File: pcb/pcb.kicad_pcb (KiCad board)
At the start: 2 copper layers, 109 x 54 mm, 63 parts, among them J1 MALE, J10 TC2030_NL, J101 MALE, J102 FEMALE, J103 MALE, J104 FEMALE, J105 MALE, J106 FEMALE, J107 MALE, J108 FEMALE, J11 STANDOFF, J111 STANDOFF, J112 STANDOFF, J113 STANDOFF, J114 STANDOFF, J12 STANDOFF, J13 STANDOFF, J14 STANDOFF, J2 FEMALE, J3 MALE, J4 FEMALE, J5 MALE, J6 FEMALE, J7 MALE, J8 FEMALE, J9 DTR, Q1 2N3904, SW1 ACTION, SW2 ACTION, SW3 ACTION, SW4 ACTION, U3 ATmega328P-MU, Y1 YSX321SL

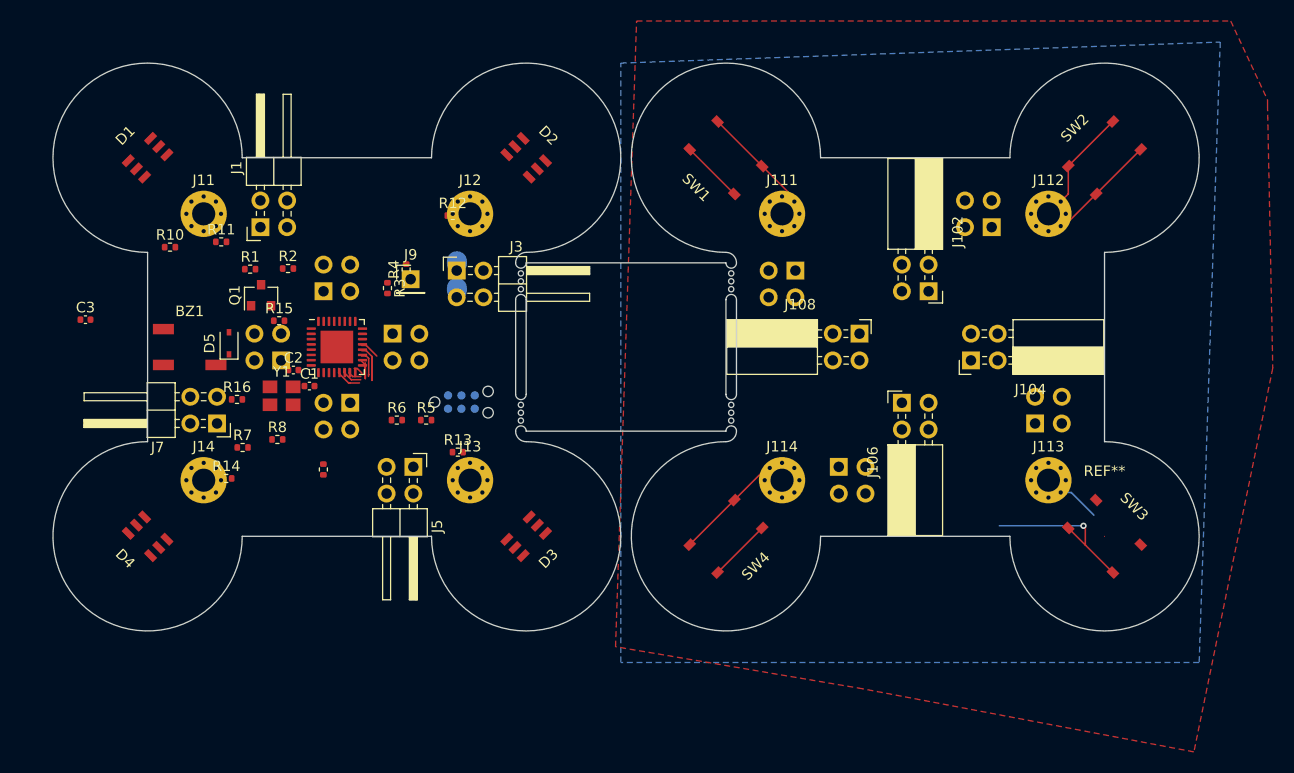
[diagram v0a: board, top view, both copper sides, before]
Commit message: Update solder mask keep out
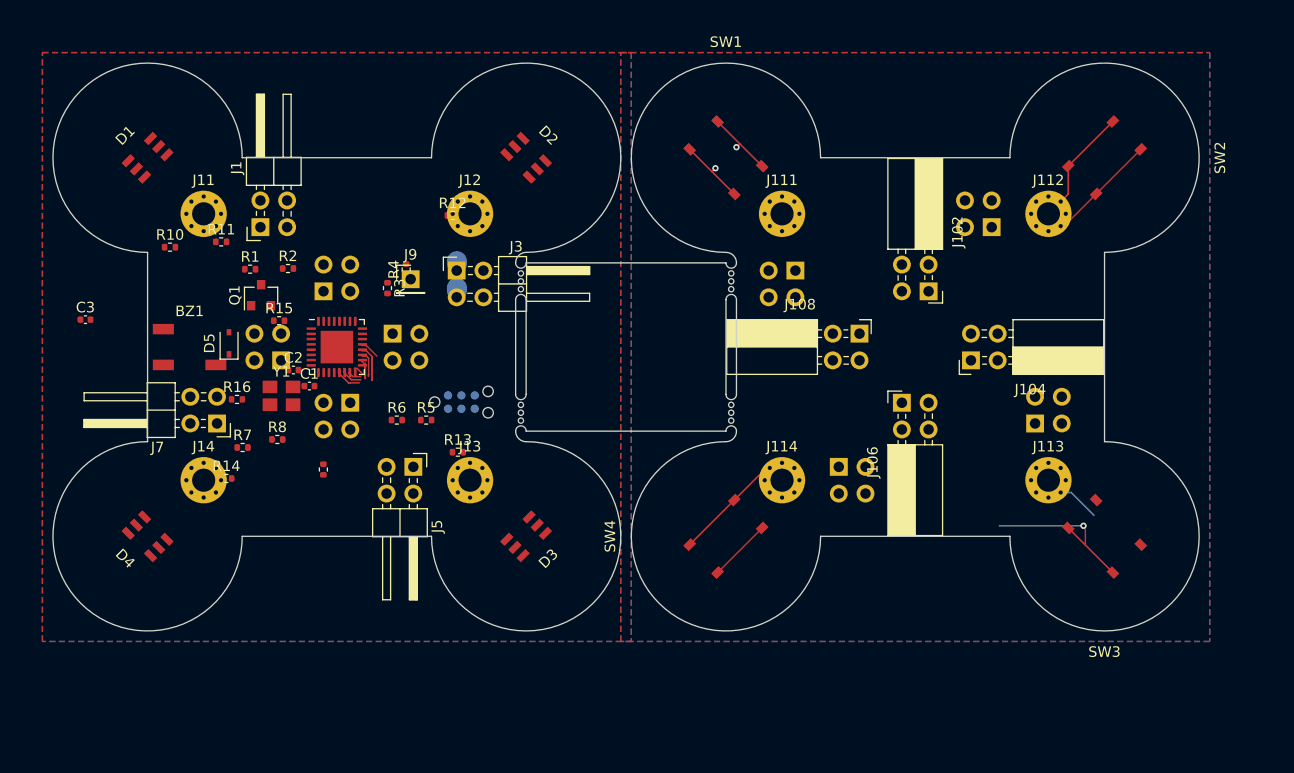
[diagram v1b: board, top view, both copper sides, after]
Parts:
- removed REF**: Leaf, node:Leaf
- SW1, SW2, SW3, SW4: footprint node:TS-1187A-B-A-B -> node:top-leaf
- turned SW1 to 0 degrees
- turned SW2 to 270 degrees
- turned SW3 to 180 degrees
- turned SW4 to 90 degrees
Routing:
- net Net-(J111-Pad1): track 16.6 -> 6.78 mm, vias 0 -> 1
- net GND: track 15.9 -> 22.4 mm, vias 1 -> 2
- added copper zone on B.Cu, net GNDB
- added copper zone on F.Cu, net GNDB
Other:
- rule pad_to_mask_clearance: 0.051 -> 0

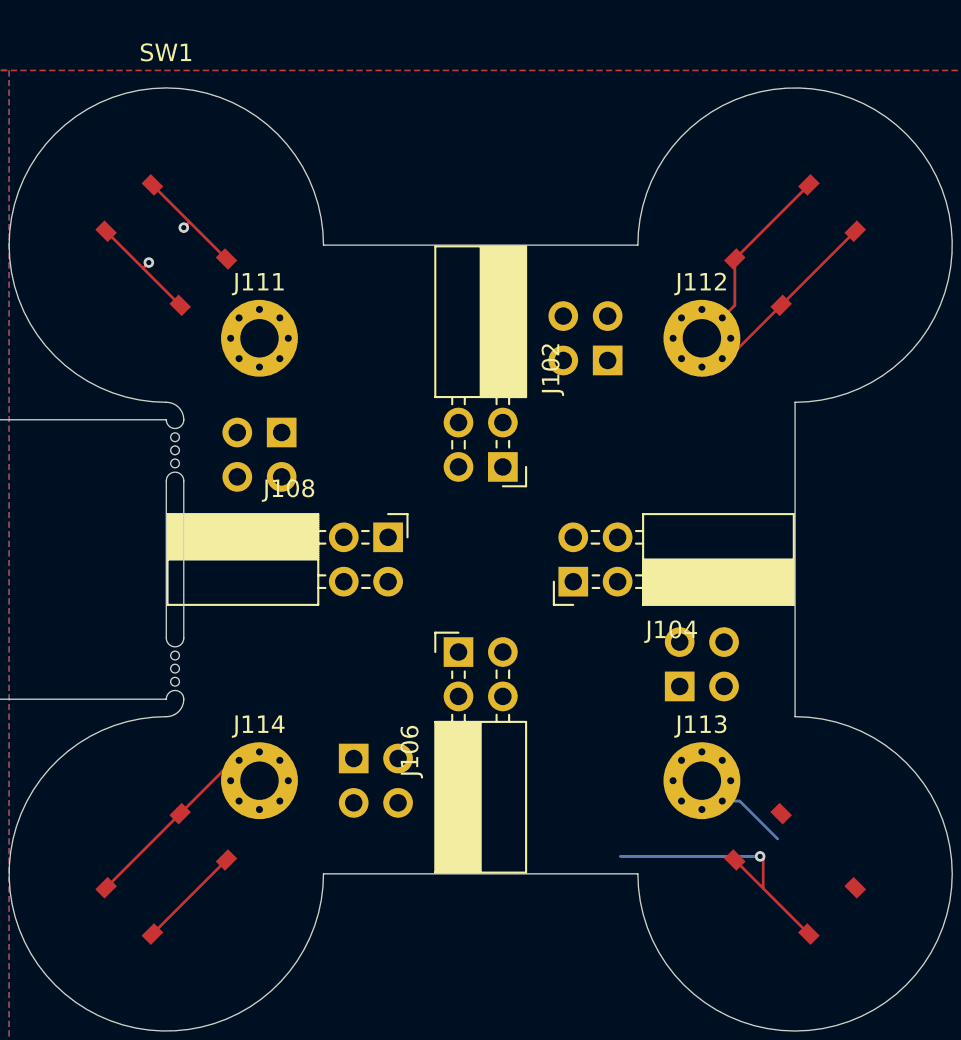
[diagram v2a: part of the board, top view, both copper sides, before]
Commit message: Route top board
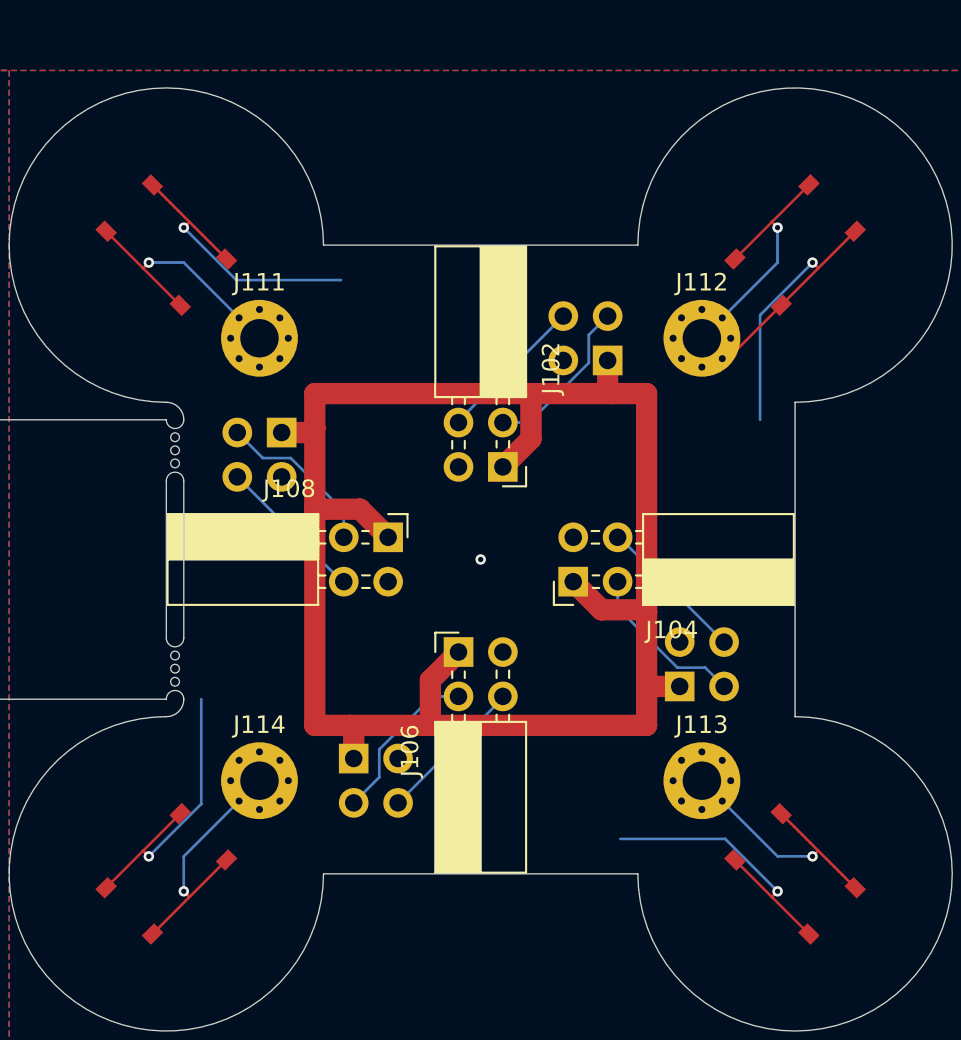
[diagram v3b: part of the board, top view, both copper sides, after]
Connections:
- J101 pad 1: Net-(J101-Pad1) -> +5V
- J102 pad 1: Net-(J101-Pad1) -> +5V
- J103 pad 1: Net-(J103-Pad1) -> +5V
- J104 pad 1: Net-(J103-Pad1) -> +5V
- J105 pad 1: Net-(J105-Pad1) -> +5V
- J106 pad 1: Net-(J105-Pad1) -> +5V
- J107 pad 1: Net-(J107-Pad1) -> +5V
- J108 pad 1: Net-(J107-Pad1) -> +5V
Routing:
- net +5V: track 0.00 -> 103.8 mm
- net GND: track 22.4 -> 50.1 mm, vias 2 -> 4
- net Net-(J112-Pad1): track 22.0 -> 35.9 mm, vias 0 -> 2
- net Net-(J113-Pad1): track 4.38 -> 14.9 mm, vias 0 -> 1
- net Net-(J107-Pad2): track 0.00 -> 9.46 mm
- net Net-(J105-Pad2): track 0.00 -> 9.46 mm
- net Net-(J103-Pad2): track 0.00 -> 9.46 mm
- net Net-(J101-Pad2): track 0.00 -> 9.46 mm
- net Net-(J107-Pad4): track 0.00 -> 8.58 mm
- net Net-(J105-Pad4): track 0.00 -> 8.58 mm
- net Net-(J103-Pad4): track 0.00 -> 8.58 mm
- net Net-(J101-Pad4): track 0.00 -> 8.58 mm
- net Net-(J111-Pad1): track 6.78 -> 13.3 mm
- net Net-(J114-Pad1): track 16.6 -> 14.9 mm, vias 0 -> 1

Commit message: Reduce footprint of tab
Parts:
- removed the mouse-bite at (138.5, 98.8)
- removed the mouse-bite at (158.5, 98.8)
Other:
- outline, holes or cut-outs redrawn
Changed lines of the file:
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@@
   (general
     (thickness 1)
-    (drawings 104)
+    (drawings 112)
     (tracks 141)
     (zones 0)
-    (modules 62)
+    (modules 60)
     (nets 70)
   )
@@
   (layers
     (0 F.Cu signal)
-    (31 B.Cu signal)
+    (31 B.Cu signal hide)
     (32 B.Adhes user hide)
     (33 F.Adhes user hide)
@@
     (38 B.Mask user hide)
     (39 F.Mask user hide)
-    (40 Dwgs.User user)
+    (40 Dwgs.User user hide)
     (41 Cmts.User user hide)
     (42 Eco1.User user hide)
@@
   )
   (module node:mouse-bite (layer F.Cu)
-    (at 138.5 98.75 90)
-    (fp_text reference mouse-bite (at 0 1.524 90) (layer F.SilkS) hide
-      (effects (font (size 1 1) (thickness 0.2)))
-    )
-    (fp_text value VAL** (at 0 -1.524 90) (layer F.SilkS) hide
-      (effects (font (size 1 1) (thickness 0.2)))
-    )
-    (fp_arc (start -1.75 0) (end -1.75 0.5) (angle -180) (layer Eco1.User) (width 0.1016))
-    (fp_arc (start 1.75 0) (end 1.75 -0.5) (angle -180) (layer Eco1.User) (width 0.1016))
-    (pad "" np_thru_hole circle (at 0 0 90) (size 0.5 0.5) (drill 0.5) (layers *.Cu *.Mask))
-    (pad "" np_thru_hole circle (at 0.75 0 90) (size 0.5 0.5) (drill 0.5) (layers *.Cu *.Mask))
-    (pad "" np_thru_hole circle (at -0.75 0 90) (size 0.5 0.5) (drill 0.5) (layers *.Cu *.Mask))
-  )
-  (module node:mouse-bite (layer F.Cu)
-    (at 158.5 98.75 90)
-    (fp_text reference mouse-bite (at 0 1.524 90) (layer F.SilkS) hide
-      (effects (font (size 1 1) (thickness 0.2)))
-    )
-    (fp_text value VAL** (at 0 -1.524 90) (layer F.SilkS) hide
-      (effects (font (size 1 1) (thickness 0.2)))
-    )
-    (fp_arc (start -1.75 0) (end -1.75 0.5) (angle -180) (layer Eco1.User) (width 0.1016))
-    (fp_arc (start 1.75 0) (end 1.75 -0.5) (angle -180) (layer Eco1.User) (width 0.1016))
-    (pad "" np_thru_hole circle (at 0 0 90) (size 0.5 0.5) (drill 0.5) (layers *.Cu *.Mask))
-    (pad "" np_thru_hole circle (at 0.75 0 90) (size 0.5 0.5) (drill 0.5) (layers *.Cu *.Mask))
-    (pad "" np_thru_hole circle (at -0.75 0 90) (size 0.5 0.5) (drill 0.5) (layers *.Cu *.Mask))
-  )
-  (module node:mouse-bite (layer F.Cu)
     (at 158.5 111.25 90)
     (fp_text reference mouse-bite (at 0 1.524 90) (layer F.SilkS) hide
@@
       (net 64 "Net-(J114-Pad1)"))
   )
-  (gr_line (start 158 113) (end 139 113) (layer Edge.Cuts) (width 0.05))
-  (gr_line (start 139 97) (end 158 97) (layer Edge.Cuts) (width 0.05))
-  (gr_line (start 138 100.5) (end 138 109.5) (layer Edge.Cuts) (width 0.05))
-  (gr_line (start 139 109.5) (end 139 100.5) (layer Edge.Cuts) (width 0.05))
-  (gr_line (start 159 100.5) (end 159 109.5) (layer Edge.Cuts) (width 0.05))
-  (gr_line (start 158 109.5) (end 158 100.5) (layer Edge.Cuts) (width 0.05))
-  (gr_arc (start 158.5 113) (end 159 113) (angle -180) (layer Edge.Cuts) (width 0.05))
-  (gr_arc (start 158.5 100.5) (end 159 100.5) (angle -180) (layer Edge.Cuts) (width 0.05))
-  (gr_arc (start 138.5 100.5) (end 139 100.5) (angle -180) (layer Edge.Cuts) (width 0.05))
-  (gr_arc (start 138.5 113) (end 139 113) (angle -180) (layer Edge.Cuts) (width 0.05))
-  (gr_line (start 130 123) (end 112 123) (layer Edge.Cuts) (width 0.05))
-  (gr_line (start 103 114) (end 103 96) (layer Edge.Cuts) (width 0.05))
-  (gr_line (start 112 87) (end 130 87) (layer Edge.Cuts) (width 0.05))
-  (gr_arc (start 103 87) (end 112 87) (angle -270) (layer Edge.Cuts) (width 0.05))
-  (gr_line (start 167 87) (end 185 87) (layer Edge.Cuts) (width 0.05))
-  (gr_line (start 194 96) (end 194 114) (layer Edge.Cuts) (width 0.05))
-  (gr_line (start 185 123) (end 167 123) (layer Edge.Cuts) (width 0.05))
-  (gr_arc (start 103 123) (end 102.999999 113.999999) (angle -270) (layer Edge.Cuts) (width 0.05))
-  (gr_arc (start 139 123) (end 130 123) (angle -270) (layer Edge.Cuts) (width 0.05))
-  (gr_arc (start 139 86.999999) (end 139 96) (angle -270) (layer Edge.Cuts) (width 0.05))
-  (gr_arc (start 139 97) (end 139 96) (angle -90) (layer Edge.Cuts) (width 0.05))
-  (gr_arc (start 158 87) (end 167 87) (angle -270) (layer Edge.Cuts) (width 0.05))
-  (gr_arc (start 158 123) (end 157.999999 113.999999) (angle -270) (layer Edge.Cuts) (width 0.05))
-  (gr_arc (start 194 123) (end 185 123) (angle -270) (layer Edge.Cuts) (width 0.05))
-  (gr_arc (start 194 86.999999) (end 194 96) (angle -270) (layer Edge.Cuts) (width 0.05))
-  (gr_arc (start 158 113) (end 158 114) (angle -90) (layer Edge.Cuts) (width 0.05))
-  (gr_arc (start 139 113) (end 138 113) (angle -90) (layer Edge.Cuts) (width 0.05))
-  (gr_arc (start 158 97) (end 159 97) (angle -90) (layer Edge.Cuts) (width 0.05))
-  (gr_arc (start 138.5 97) (end 138 97) (angle -180) (layer Edge.Cuts) (width 0.05))
-  (gr_arc (start 158.5 97) (end 158 97) (angle -180) (layer Edge.Cuts) (width 0.05))
-  (gr_arc (start 158.5 109.5) (end 158 109.5) (angle -180) (layer Edge.Cuts) (width 0.05))
-  (gr_arc (start 138.5 109.5) (end 138 109.5) (angle -180) (layer Edge.Cuts) (width 0.05))
+  (gr_line (start 158.050126 109.5) (end 139.050126 109.5) (layer Edge.Cuts) (width 0.05))
+  (gr_arc (start 138.550126 109.5) (end 138.050126 109.5) (angle -180) (layer Edge.Cuts) (width 0.05))
+  (gr_arc (start 158.050126 109.5) (end 159.050126 109.5) (angle -90) (layer Edge.Cuts) (width 0.05))
+  (gr_arc (start 158.550126 109.5) (end 158.050126 109.5) (angle -180) (layer Edge.Cuts) (width 0.05))
+  (gr_line (start 129.100251 87) (end 113 87) (layer Edge.Cuts) (width 0.05))
+  (gr_arc (start 139.050126 109.5) (end 139.050126 108.5) (angle -90) (layer Edge.Cuts) (width 0.05))
+  (gr_line (start 158.050126 96.949874) (end 158.050126 108.5) (layer Edge.Cuts) (width 0.05))
+  (gr_arc (start 129.100251 86) (end 129.100251 87) (angle -84.26082952) (layer Edge.Cuts) (width 0.05))
+  (gr_arc (start 139.050126 86.999999) (end 139.950126 95.954886) (angle -258.521659) (layer Edge.Cuts) (width 0.05))
+  (gr_arc (start 140.050126 96.949874) (end 139.950126 95.954886) (angle -84.26082952) (layer Edge.Cuts) (width 0.05))
+  (gr_line (start 139.050126 108.5) (end 139.050126 96.949874) (layer Edge.Cuts) (width 0.05))
+  (gr_arc (start 139.050126 123) (end 130.095239 123.9) (angle -264.2608295) (layer Edge.Cuts) (width 0.05))
+  (gr_arc (start 102.050126 96.949874) (end 103.050126 96.949874) (angle -84.26082952) (layer Edge.Cuts) (width 0.05))
+  (gr_arc (start 129.100251 124) (end 130.095239 123.9) (angle -84.26082952) (layer Edge.Cuts) (width 0.05))
+  (gr_line (start 113 123) (end 129.100251 123) (layer Edge.Cuts) (width 0.05))
+  (gr_arc (start 103.050125 87) (end 112.005012 86.1) (angle -258.521659) (layer Edge.Cuts) (width 0.05))
+  (gr_arc (start 113 124) (end 113 123) (angle -84.26082952) (layer Edge.Cuts) (width 0.05))
+  (gr_arc (start 103.050125 123) (end 102.150125 114.045113) (angle -258.521659) (layer Edge.Cuts) (width 0.05))
+  (gr_arc (start 102.050126 113.050125) (end 102.150126 114.045113) (angle -84.26082952) (layer Edge.Cuts) (width 0.05))
+  (gr_line (start 103.050126 96.949874) (end 103.050126 113.050125) (layer Edge.Cuts) (width 0.05))
+  (gr_arc (start 113 86) (end 112.005012 86.1) (angle -84.26082952) (layer Edge.Cuts) (width 0.05))
+  (gr_arc (start 194.050126 123) (end 185.095239 123.899999) (angle -258.521659) (layer Edge.Cuts) (width 0.05))
+  (gr_arc (start 195.050126 113.050125) (end 194.050126 113.050125) (angle -84.26082952) (layer Edge.Cuts) (width 0.05))
+  (gr_arc (start 184.100251 86) (end 184.100251 86.999999) (angle -84.26082952) (layer Edge.Cuts) (width 0.05))
+  (gr_arc (start 194.050126 87) (end 194.950126 95.954886) (angle -258.521659) (layer Edge.Cuts) (width 0.05))
+  (gr_arc (start 157.050126 96.949874) (end 158.050126 96.949874) (angle -84.26082952) (layer Edge.Cuts) (width 0.05))
+  (gr_arc (start 195.050126 96.949874) (end 194.950126 95.954886) (angle -84.26082952) (layer Edge.Cuts) (width 0.05))
+  (gr_arc (start 158.050125 87) (end 167.005012 86.1) (angle -258.521659) (layer Edge.Cuts) (width 0.05))
+  (gr_arc (start 168 86) (end 167.005012 86.1) (angle -84.26082952) (layer Edge.Cuts) (width 0.05))
+  (gr_line (start 184.100251 86.999999) (end 168 87) (layer Edge.Cuts) (width 0.05))
+  (gr_line (start 194.050126 113.050125) (end 194.050126 96.949874) (layer Edge.Cuts) (width 0.05))
+  (gr_arc (start 184.100251 124) (end 185.095239 123.899999) (angle -84.26082952) (layer Edge.Cuts) (width 0.05))
+  (gr_arc (start 168 123.999999) (end 168 123) (angle -84.26082952) (layer Edge.Cuts) (width 0.05))
+  (gr_line (start 139.050126 113) (end 158.050126 113) (layer Edge.Cuts) (width 0.05))
+  (gr_arc (start 158.050126 122.999999) (end 158.050126 114) (angle -264.2608295) (layer Edge.Cuts) (width 0.05))
+  (gr_arc (start 158.050126 113) (end 158.050126 114) (angle -90) (layer Edge.Cuts) (width 0.05))
+  (gr_arc (start 158.550126 113) (end 159.050126 113) (angle -180) (layer Edge.Cuts) (width 0.05))
+  (gr_arc (start 138.550126 113) (end 139.050126 113) (angle -180) (layer Edge.Cuts) (width 0.05))
+  (gr_arc (start 139.050126 113) (end 138.050126 113) (angle -90) (layer Edge.Cuts) (width 0.05))
+  (gr_line (start 168 123) (end 184.100251 123) (layer Edge.Cuts) (width 0.05))
   (gr_circle (center 189.935999 112.269999) (end 190.935999 112.269999) (layer Dwgs.User) (width 0.05))
   (gr_circle (center 187.395999 112.269999) (end 188.395999 112.269999) (layer Dwgs.User) (width 0.05))

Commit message: Position bottom-leaf footprints
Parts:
- D1, D2, D3, D4: footprint node:WS2813-Mini -> node:bottom-leaf
- turned D1 to 0 degrees
- turned D2 to 270 degrees
- turned D3 to 180 degrees
- turned D4 to 90 degrees
